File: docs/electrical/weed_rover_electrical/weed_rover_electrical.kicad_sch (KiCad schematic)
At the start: 20 parts, among them J1 Motors JST, SW1 Main switch, SW2 Key lock, SW3 Emergency stop, U1 Raspberry Pi 5, U10 VL53L0X front, U11 VL53L0X rear, U2 ESP32-WROOM-32E, U3 Mini560 5V/5A, U4 INA219, U5 MD13S left, U6 MD13S right, U7 Laser driver + nFET, U8 HC-SR04 front-left, U9 HC-SR04 front-right

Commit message: feat(design): 3-DOF laser arm — mechanical CAD + servo wiring
Mechanical (docs/mechanical/laser_arm):
- FreeCAD-built assembly, 28 named parts (STL + per-part STEP)
- Yaw turret (MG996R) -> shoulder (DS3218) -> elbow (DS3218) -> 445nm head
- L1=160mm L2=140mm, tip 351mm forward / 78mm above deck at neutral pose
- Torque checks: shoulder 5.4 kg-cm vs 20 rated; yaw covered by MG996R
- Weeding pose: tip reaches ground ~285mm ahead of the turret

Electrical (docs/electrical/weed_rover_electrical):
- Added servo PWM nets PWM_YAW/PWM_SH/PWM_EL from the ESP32
- Added U15 UBEC 6V/10A on +6VS rail (servo power isolated from Pi 5V)
- ERC re-run: 0 errors, 37 nets; PDF/PNG/netlist regenerated
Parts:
- added U12: Servo yaw MG996R, symbol U12
- added U13: Servo shoulder DS3218, symbol U13
- added U14: Servo elbow DS3218, symbol U14
- added U15: UBEC 6V 10A, symbol U15
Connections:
- net +12VL: now also U15.1 (+12VL)
- net BAT_ADC: now also U2.14 (BAT_ADC); no longer U2.11 (BAT_ADC)
- net GND: now also U12.3 (GND), U13.3 (GND), U14.3 (GND), U15.2 (GND), U15.4 (GND)
- net MTR_ERR: now also U2.15 (MTR_ERR); no longer U2.12 (MTR_ERR)
- new net +6VS: U12.2 (+6VS), U13.2 (+6VS), U14.2 (+6VS), U15.3 (+6VS)
- new net PWM_EL: U14.1 (PWM_EL), U2.13 (PWM_EL)
- new net PWM_SH: U13.1 (PWM_SH), U2.12 (PWM_SH)
- new net PWM_YAW: U12.1 (PWM_YAW), U2.11 (PWM_YAW)

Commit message: Electrical: fully wired schematic - routed wires for all 37 nets, junction dots, tidy servo row, PNG+PDF exports
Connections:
- net +12VL is gone; now on net +12V: U15.1 (+12VL), U3.1 (+12VL), U4.2 (+12VL), U5.1 (+12VL), U6.1 (+12VL), U7.1 (+12VL)
- net +5V is gone; now on net +12V: D2.1 (+5V), U1.1 (+5V), U3.3 (+5V), U8.1 (+5V), U9.1 (+5V)
- net +6VS is gone; now on net +12V: U12.2 (+6VS), U13.2 (+6VS), U14.2 (+6VS), U15.3 (+6VS)
- net 3V3 is gone; now on net +12V: LS1.2 (3V3), SW2.1 (3V3), SW3.1 (3V3), U1.22 (3V3), U10.1 (3V3), U11.1 (3V3), U2.1 (3V3), U4.6 (3V3)
- net BAT_ADC is gone; now on net +12V: U1.14 (BAT_ADC), U2.14 (BAT_ADC)
- net BUZZ is gone; now on net +12V: LS1.1 (BUZZ), U1.21 (BUZZ)
- net DIR_L is gone; now on net +12V: U1.9 (DIR_L), U2.8 (DIR_L), U5.4 (DIR_L)
- net DIR_R is gone; now on net +12V: U1.10 (DIR_R), U2.9 (DIR_R), U6.4 (DIR_R)
- net ECHO_L is gone; now on net +12V: U1.17 (ECHO_L), U8.4 (ECHO_L)
- net ECHO_R is gone; now on net +12V: U1.18 (ECHO_R), U9.4 (ECHO_R)
- net ESTOP_N is gone; now on net +12V: SW3.2 (ESTOP_N), U1.20 (ESTOP_N), U2.5 (ESTOP_N)
- net GND is gone; now on net +12V: BT1.2 (GND), D2.2 (GND), LS1.3 (GND), SW3.3 (GND), U1.2 (GND), U1.23 (GND), U10.2 (GND), U11.2 (GND), U12.3 (GND), U13.3 (GND), U14.3 (GND), U15.2 (GND), U15.4 (GND), U2.2 (GND), U3.2 (GND), U3.4 (GND), U4.3 (GND), U5.2 (GND), U6.2 (GND), U7.2 (GND), U8.2 (GND), U9.2 (GND)
- net LASER_EN is gone; now on net +12V: U1.11 (LASER_EN), U2.10 (LASER_EN), U7.3 (LASER_EN)
- net MTR_ERR is gone; now on net +12V: U1.19 (MTR_ERR), U2.15 (MTR_ERR)
- net PWM_EL is gone; now on net +12V: U14.1 (PWM_EL), U2.13 (PWM_EL)
- net PWM_L is gone; now on net +12V: U1.7 (PWM_L), U2.6 (PWM_L), U5.3 (PWM_L)
- net PWM_R is gone; now on net +12V: U1.8 (PWM_R), U2.7 (PWM_R), U6.3 (PWM_R)
- net PWM_SH is gone; now on net +12V: U13.1 (PWM_SH), U2.12 (PWM_SH)
- net PWM_YAW is gone; now on net +12V: U12.1 (PWM_YAW), U2.11 (PWM_YAW)
- net SCL is gone; now on net +12V: U1.4 (SCL), U10.4 (SCL), U11.4 (SCL), U4.5 (SCL)
- net SDA is gone; now on net +12V: U1.3 (SDA), U10.3 (SDA), U11.3 (SDA), U4.4 (SDA)
- net TRIG_L is gone; now on net +12V: U1.15 (TRIG_L), U8.3 (TRIG_L)
- net TRIG_R is gone; now on net +12V: U1.16 (TRIG_R), U9.3 (TRIG_R)
- net UART_RX is gone; now on net +12V: U1.6 (UART_RX), U2.4 (UART_RX)
- net UART_TX is gone; now on net +12V: U1.5 (UART_TX), U2.3 (UART_TX)
- net XSHUT_L is gone; now on net +12V: U1.12 (XSHUT_L), U10.5 (XSHUT_L)
- net XSHUT_R is gone; now on net +12V: U1.13 (XSHUT_R), U11.5 (XSHUT_R)

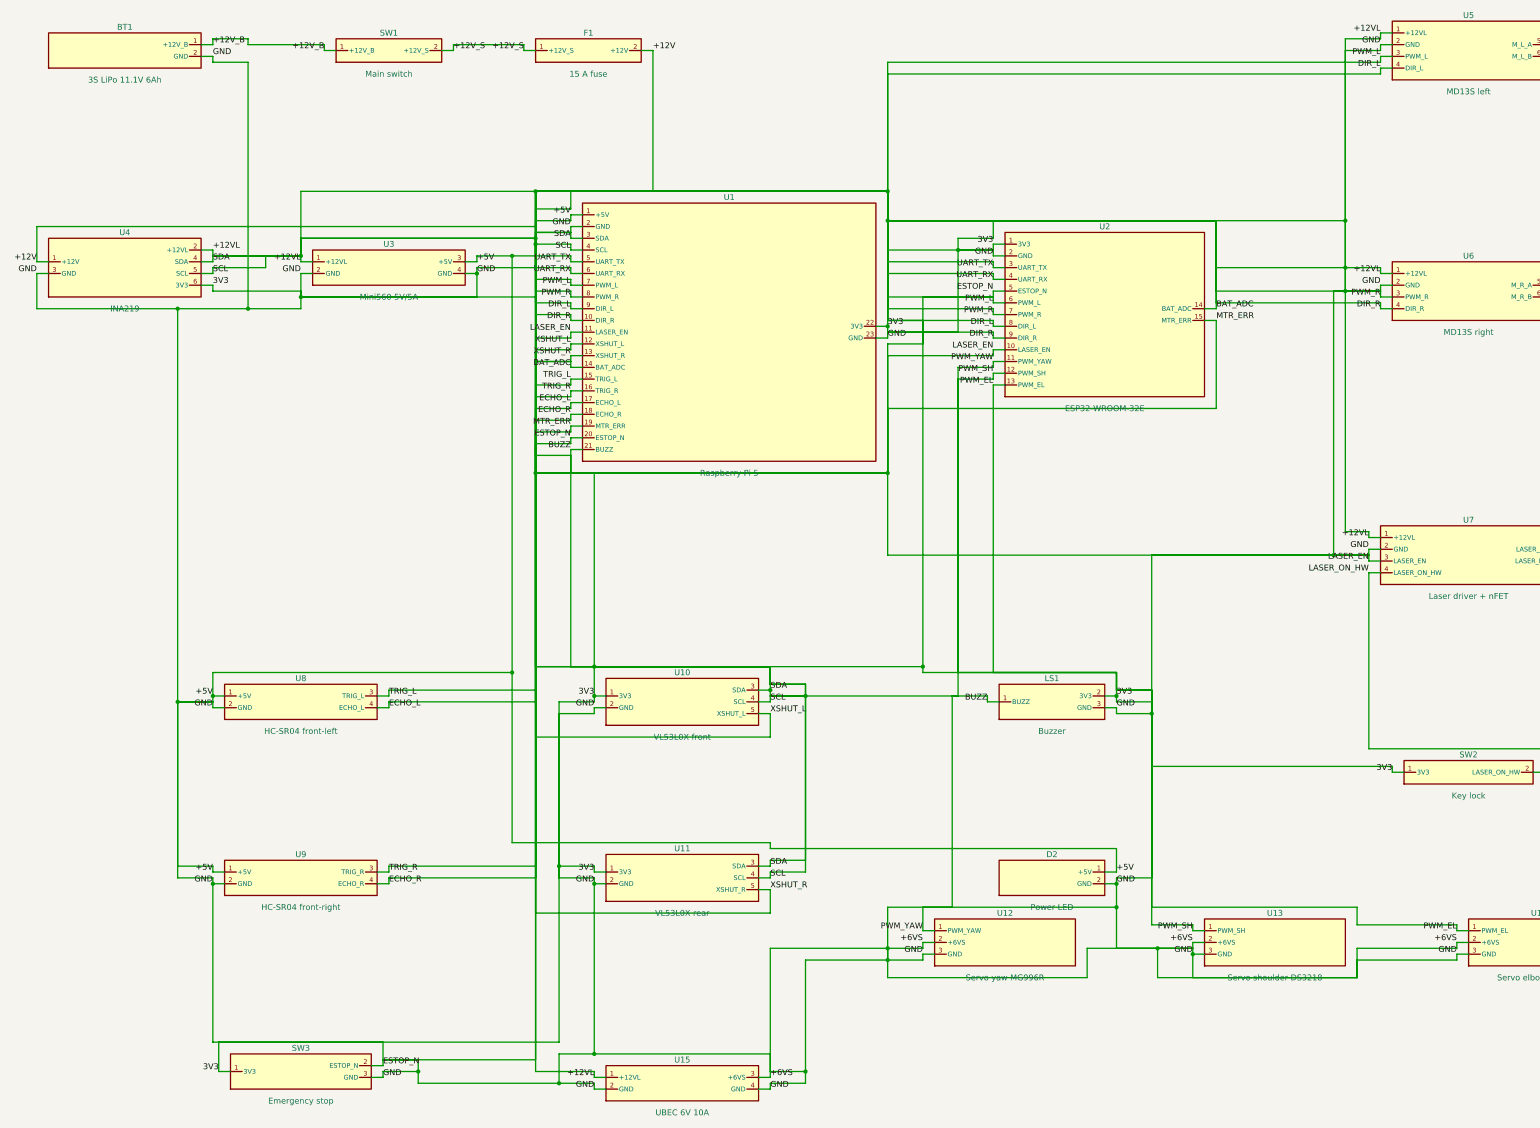
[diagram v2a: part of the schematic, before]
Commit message: paper: IEEE conference draft + reproducible benchmark suite; fix electrical mega-net
- Navigation/benchmarks/: synthetic-field tilt robustness benchmark
  (tilt 0-60 deg x {1.2, 0.6 m} pitch x 8 seeds, raw vs regularize ablation,
  corner-tap noise sweep) with results in docs/paper/results/
- docs/paper/: 6-page IEEEtran draft (paper.tex + paper.pdf) with real
  measured numbers, authentic figures (real-field triptych, outbox plan
  overlay, sim stills, KiCad schematic), verified 8-entry bibliography
- electrical fix: make_schematic.py router never claimed routed cells, so
  different nets shared free corridor cells and KiCad merged them into one
  mega-net; claim() is now called per net. Netlist exports all 37 intended
  nets; ERC reports zero connectivity violations (remaining flags are
  symbol-library table notices). PNG/PDF re-exported.
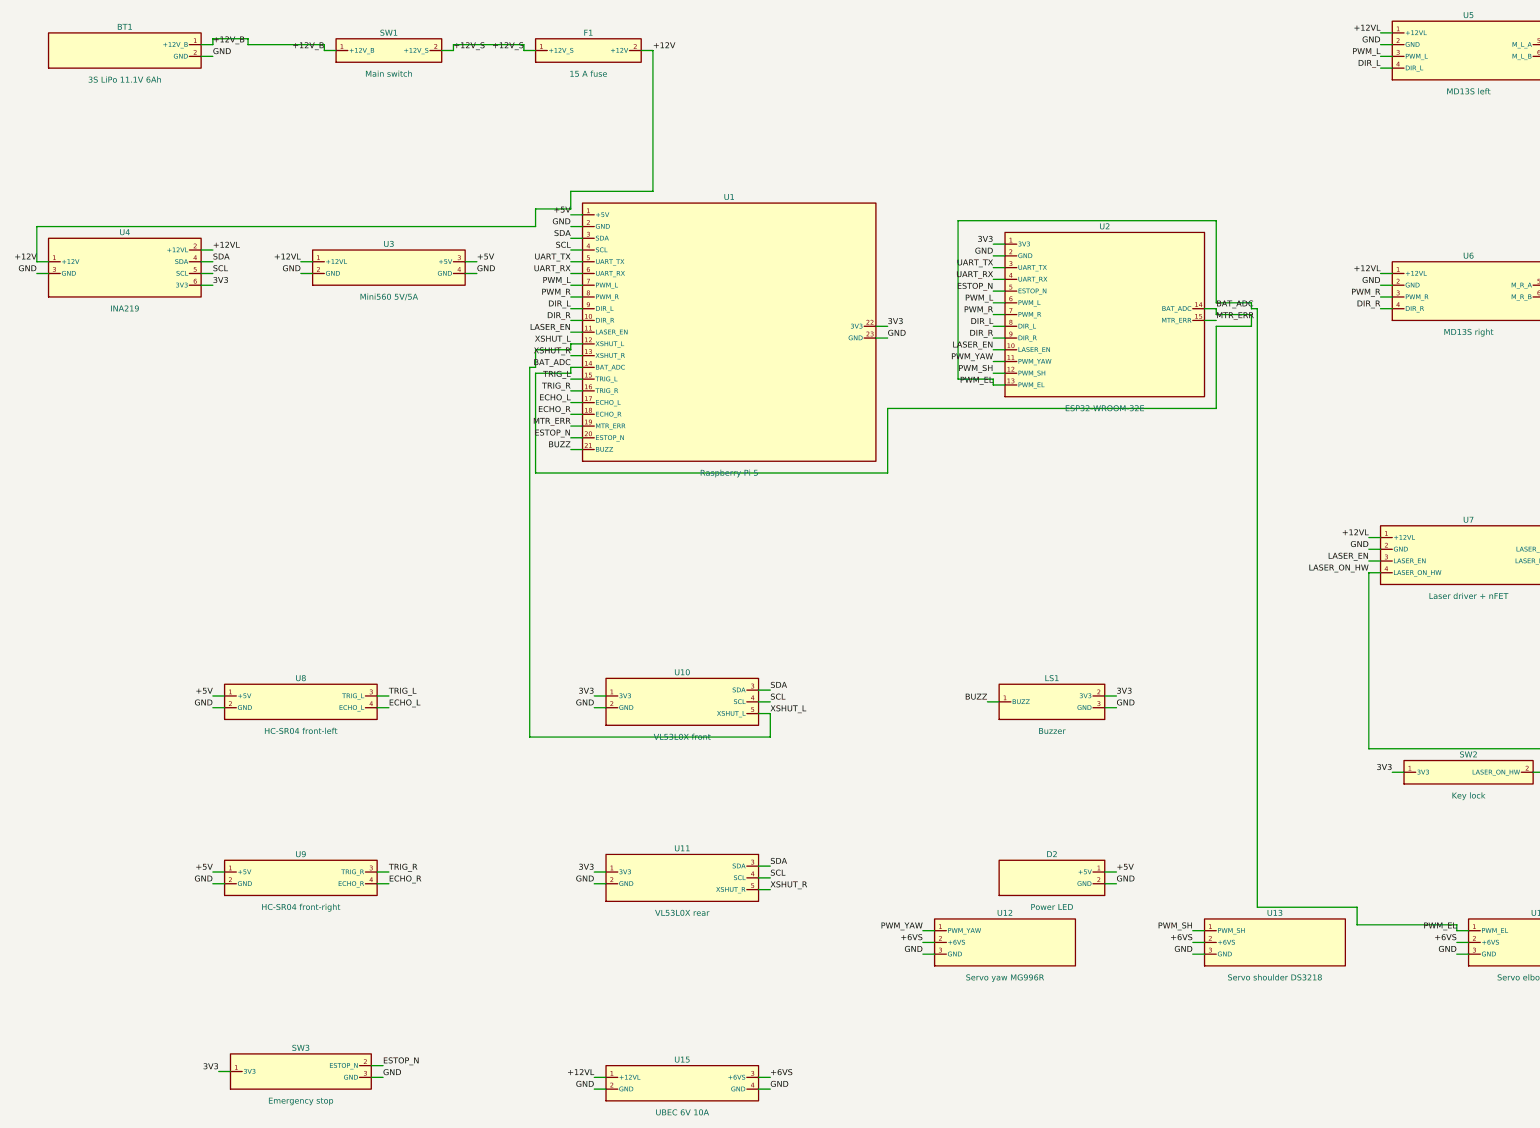
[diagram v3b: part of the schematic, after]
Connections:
- net +12V: no longer BT1.2 (GND), D2.1 (+5V), D2.2 (GND), LS1.1 (BUZZ), LS1.2 (3V3), LS1.3 (GND), SW2.1 (3V3), SW3.1 (3V3), SW3.2 (ESTOP_N), SW3.3 (GND), U1.1 (+5V), U1.10 (DIR_R), U1.11 (LASER_EN), U1.12 (XSHUT_L), U1.13 (XSHUT_R), U1.14 (BAT_ADC), U1.15 (TRIG_L), U1.16 (TRIG_R), U1.17 (ECHO_L), U1.18 (ECHO_R), U1.19 (MTR_ERR), U1.2 (GND), U1.20 (ESTOP_N), U1.21 (BUZZ), U1.22 (3V3), U1.23 (GND), U1.3 (SDA), U1.4 (SCL), U1.5 (UART_TX), U1.6 (UART_RX), U1.7 (PWM_L), U1.8 (PWM_R), U1.9 (DIR_L), U10.1 (3V3), U10.2 (GND), U10.3 (SDA), U10.4 (SCL), U10.5 (XSHUT_L), U11.1 (3V3), U11.2 (GND), U11.3 (SDA), U11.4 (SCL), U11.5 (XSHUT_R), U12.1 (PWM_YAW), U12.2 (+6VS), U12.3 (GND), U13.1 (PWM_SH), U13.2 (+6VS), U13.3 (GND), U14.1 (PWM_EL), U14.2 (+6VS), U14.3 (GND), U15.1 (+12VL), U15.2 (GND), U15.3 (+6VS), U15.4 (GND), U2.1 (3V3), U2.10 (LASER_EN), U2.11 (PWM_YAW), U2.12 (PWM_SH), U2.13 (PWM_EL), U2.14 (BAT_ADC), U2.15 (MTR_ERR), U2.2 (GND), U2.3 (UART_TX), U2.4 (UART_RX), U2.5 (ESTOP_N), U2.6 (PWM_L), U2.7 (PWM_R), U2.8 (DIR_L), U2.9 (DIR_R), U3.1 (+12VL), U3.2 (GND), U3.3 (+5V), U3.4 (GND), U4.2 (+12VL), U4.3 (GND), U4.4 (SDA), U4.5 (SCL), U4.6 (3V3), U5.1 (+12VL), U5.2 (GND), U5.3 (PWM_L), U5.4 (DIR_L), U6.1 (+12VL), U6.2 (GND), U6.3 (PWM_R), U6.4 (DIR_R), U7.1 (+12VL), U7.2 (GND), U7.3 (LASER_EN), U8.1 (+5V), U8.2 (GND), U8.3 (TRIG_L), U8.4 (ECHO_L), U9.1 (+5V), U9.2 (GND), U9.3 (TRIG_R), U9.4 (ECHO_R)
- new net +12VL: U15.1 (+12VL), U3.1 (+12VL), U4.2 (+12VL), U5.1 (+12VL), U6.1 (+12VL), U7.1 (+12VL)
- new net +5V: D2.1 (+5V), U1.1 (+5V), U3.3 (+5V), U8.1 (+5V), U9.1 (+5V)
- new net +6VS: U12.2 (+6VS), U13.2 (+6VS), U14.2 (+6VS), U15.3 (+6VS)
- new net 3V3: LS1.2 (3V3), SW2.1 (3V3), SW3.1 (3V3), U1.22 (3V3), U10.1 (3V3), U11.1 (3V3), U2.1 (3V3), U4.6 (3V3)
- new net BAT_ADC: U1.14 (BAT_ADC), U2.14 (BAT_ADC)
- new net BUZZ: LS1.1 (BUZZ), U1.21 (BUZZ)
- new net DIR_L: U1.9 (DIR_L), U2.8 (DIR_L), U5.4 (DIR_L)
- new net DIR_R: U1.10 (DIR_R), U2.9 (DIR_R), U6.4 (DIR_R)
- new net ECHO_L: U1.17 (ECHO_L), U8.4 (ECHO_L)
- new net ECHO_R: U1.18 (ECHO_R), U9.4 (ECHO_R)
- new net ESTOP_N: SW3.2 (ESTOP_N), U1.20 (ESTOP_N), U2.5 (ESTOP_N)
- new net GND: BT1.2 (GND), D2.2 (GND), LS1.3 (GND), SW3.3 (GND), U1.2 (GND), U1.23 (GND), U10.2 (GND), U11.2 (GND), U12.3 (GND), U13.3 (GND), U14.3 (GND), U15.2 (GND), U15.4 (GND), U2.2 (GND), U3.2 (GND), U3.4 (GND), U4.3 (GND), U5.2 (GND), U6.2 (GND), U7.2 (GND), U8.2 (GND), U9.2 (GND)
- new net LASER_EN: U1.11 (LASER_EN), U2.10 (LASER_EN), U7.3 (LASER_EN)
- new net MTR_ERR: U1.19 (MTR_ERR), U2.15 (MTR_ERR)
- new net PWM_EL: U14.1 (PWM_EL), U2.13 (PWM_EL)
- new net PWM_L: U1.7 (PWM_L), U2.6 (PWM_L), U5.3 (PWM_L)
- new net PWM_R: U1.8 (PWM_R), U2.7 (PWM_R), U6.3 (PWM_R)
- new net PWM_SH: U13.1 (PWM_SH), U2.12 (PWM_SH)
- new net PWM_YAW: U12.1 (PWM_YAW), U2.11 (PWM_YAW)
- new net SCL: U1.4 (SCL), U10.4 (SCL), U11.4 (SCL), U4.5 (SCL)
- new net SDA: U1.3 (SDA), U10.3 (SDA), U11.3 (SDA), U4.4 (SDA)
- new net TRIG_L: U1.15 (TRIG_L), U8.3 (TRIG_L)
- new net TRIG_R: U1.16 (TRIG_R), U9.3 (TRIG_R)
- new net UART_RX: U1.6 (UART_RX), U2.4 (UART_RX)
- new net UART_TX: U1.5 (UART_TX), U2.3 (UART_TX)
- new net XSHUT_L: U1.12 (XSHUT_L), U10.5 (XSHUT_L)
- new net XSHUT_R: U1.13 (XSHUT_R), U11.5 (XSHUT_R)
